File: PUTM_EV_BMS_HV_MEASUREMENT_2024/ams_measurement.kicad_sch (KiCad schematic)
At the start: 27 parts, among them J1 CELL_PAD, J10 CELL_PAD, J11 CELL_PAD, J12 Conn_02x10_Odd_Even, J2 CELL_PAD, J3 CELL_PAD, J4 CELL_PAD, J5 CELL_PAD, J6 CELL_PAD, J7 CELL_PAD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

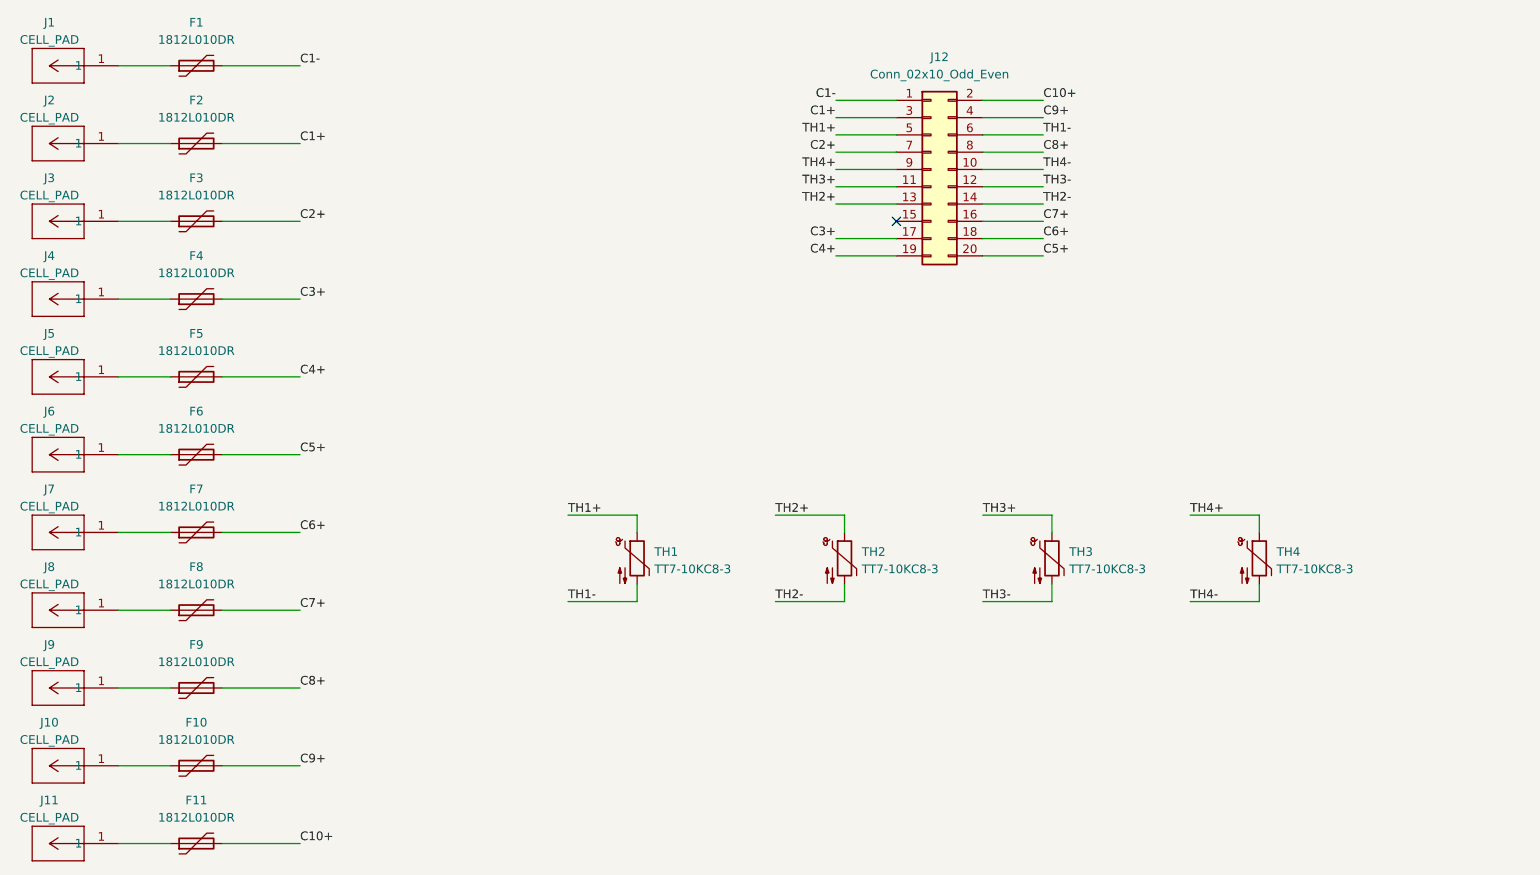
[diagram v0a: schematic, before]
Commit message: Wider tracks, vias and common -
Tracks now 1.2mm
Vias added to WAGO connector footprint
All thermistors now have common negative pin
Changes to thermistor placement (added TH5)
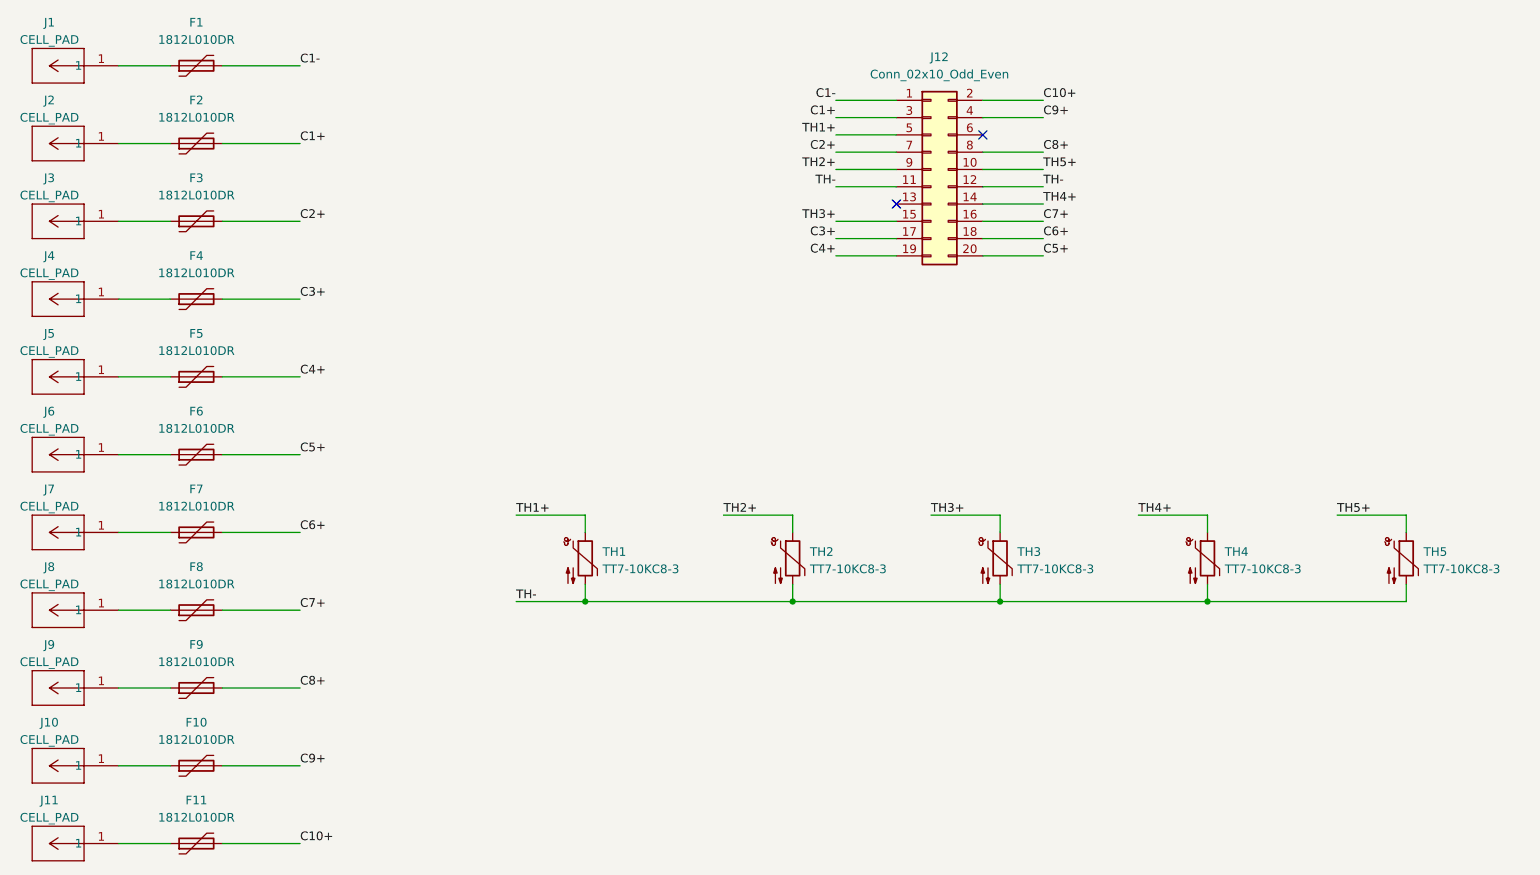
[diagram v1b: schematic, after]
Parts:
- added TH5: TT7-10KC8-3, Connector_PinHeader_2.54mm:PinHeader_1x02_P2.54mm_Vertical, symbol Device:Thermistor_NTC
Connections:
- net TH3- is gone; now on net TH-: J12.12 (Pin_12), TH3.2
- net TH2+: now also J12.9 (Pin_9); no longer J12.13 (Pin_13)
- net TH3+: now also J12.15 (Pin_15); no longer J12.11 (Pin_11)
- net TH4+: now also J12.14 (Pin_14); no longer J12.9 (Pin_9)
- net TH1-: no longer names the net of J12.6 (Pin_6)
- net TH1-: no longer TH1.2
- net TH2- renamed TH-
- net TH-: now also J12.11 (Pin_11), TH1.2, TH4.2, TH5.2; no longer J12.14 (Pin_14)
- net TH4- renamed TH5+
- net TH5+: now also TH5.1; no longer TH4.2
- no-connect marks 1 -> 2
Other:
- moved on the sheet: TH1, TH2, TH3, TH4
